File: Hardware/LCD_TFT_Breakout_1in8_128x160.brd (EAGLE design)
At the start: 40.6 x 59.7 mm, 62 parts, among them J1 MICRO-SD_CARD_SOCKETTINY, Q1 220mA/50V/3.5Ω, U2 TXB0108DQSR, U3 3.3V

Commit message: Fix silkscreen and bump out SD card 50 mil
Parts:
- moved U$14 7.62 mm to (15.2, 1.52)
- moved U$29 7.62 mm to (15.2, 1.52)
- moved U$11 2.67 mm to (17.9, 1.52)
- moved U$26 2.67 mm to (17.9, 1.52)
- moved U$12 2.54 mm to (20.3, 1.52)
- moved U$13 2.54 mm to (22.9, 1.52)
- moved U$27 2.54 mm to (20.3, 1.52)
- moved U$28 2.54 mm to (22.9, 1.52)
- moved J1 1.27 mm to (6.35, 19.1)
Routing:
- net 3.3V: track 104.1 -> 107.0 mm
- net MISO: track 23.3 -> 24.6 mm
- net SD_!CS: track 17.6 -> 18.9 mm
- net SCLK: track 30.3 -> 31.5 mm
- net MOSI: track 30.2 -> 31.4 mm
- net GND: vias 31 -> 30

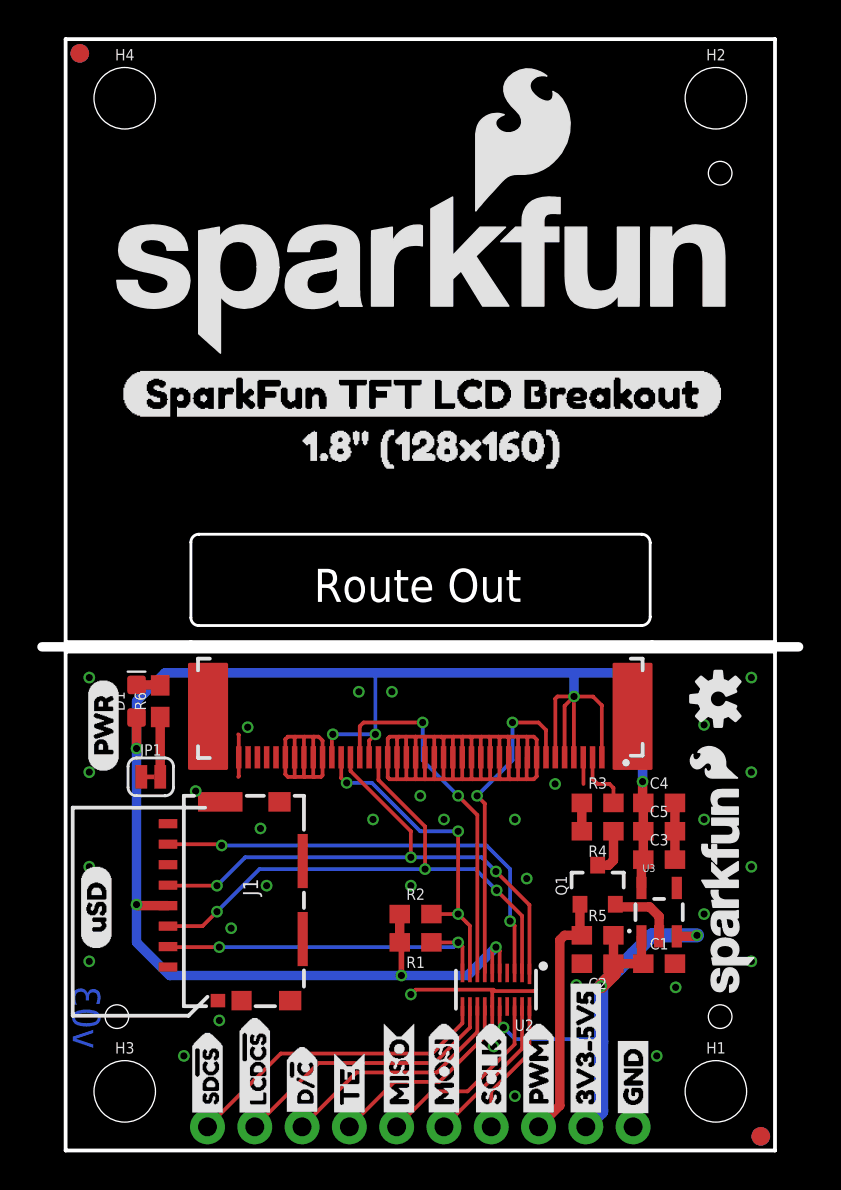
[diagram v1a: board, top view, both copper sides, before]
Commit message: Reduce strain on FPC cable
Acheived by moving the connector toward the PTH row by 40 mil. Route out area moved flush with v-score and also narrowed a little bit
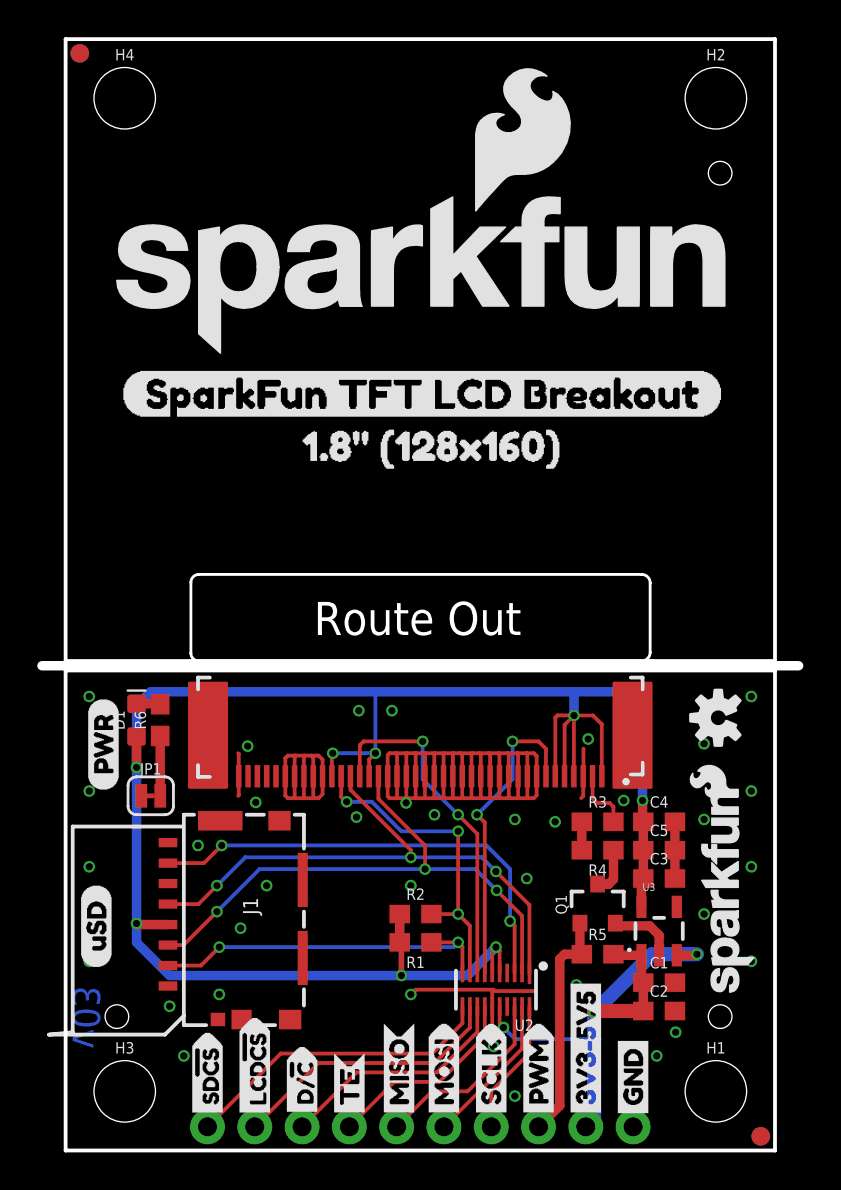
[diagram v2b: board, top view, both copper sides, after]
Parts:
- moved C2 4.17 mm to (31.9, 7.49), turned to 0 degrees
- moved C4 1.02 mm to (31.9, 17.7)
- moved J1 1.02 mm to (6.35, 18.0)
- moved LOGO3 1.02 mm to (35.1, 23.2)
- moved R3 1.02 mm to (28.6, 17.7)
- moved U$18 1.02 mm to (2.03, 19.3)
- moved U$23 1.02 mm to (31.9, 24.5)
- moved C1 1.02 mm to (31.9, 9.02)
- moved C3 1.02 mm to (31.9, 14.6)
- moved Q1 1.02 mm to (28.6, 13.2)
- moved R5 1.02 mm to (28.6, 10.5)
- moved U$4 1.02 mm to (1.65, 9.78)
- moved U3 1.02 mm to (31.9, 11.8)
- moved C5 1.02 mm to (31.9, 16.1)
- moved D1 1.02 mm to (3.81, 23.1)
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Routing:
- net GND: track 90.1 -> 94.0 mm, vias 30 -> 34
- net LED_PWM: track 13.5 -> 12.5 mm
- net D/!C: track 19.8 -> 18.8 mm
- net TE: track 17.8 -> 16.8 mm
- net SCLK: track 31.5 -> 30.9 mm
- net MOSI: track 31.4 -> 30.8 mm
- net 3.3V: track 107.0 -> 106.4 mm
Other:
- outline, holes or cut-outs redrawn

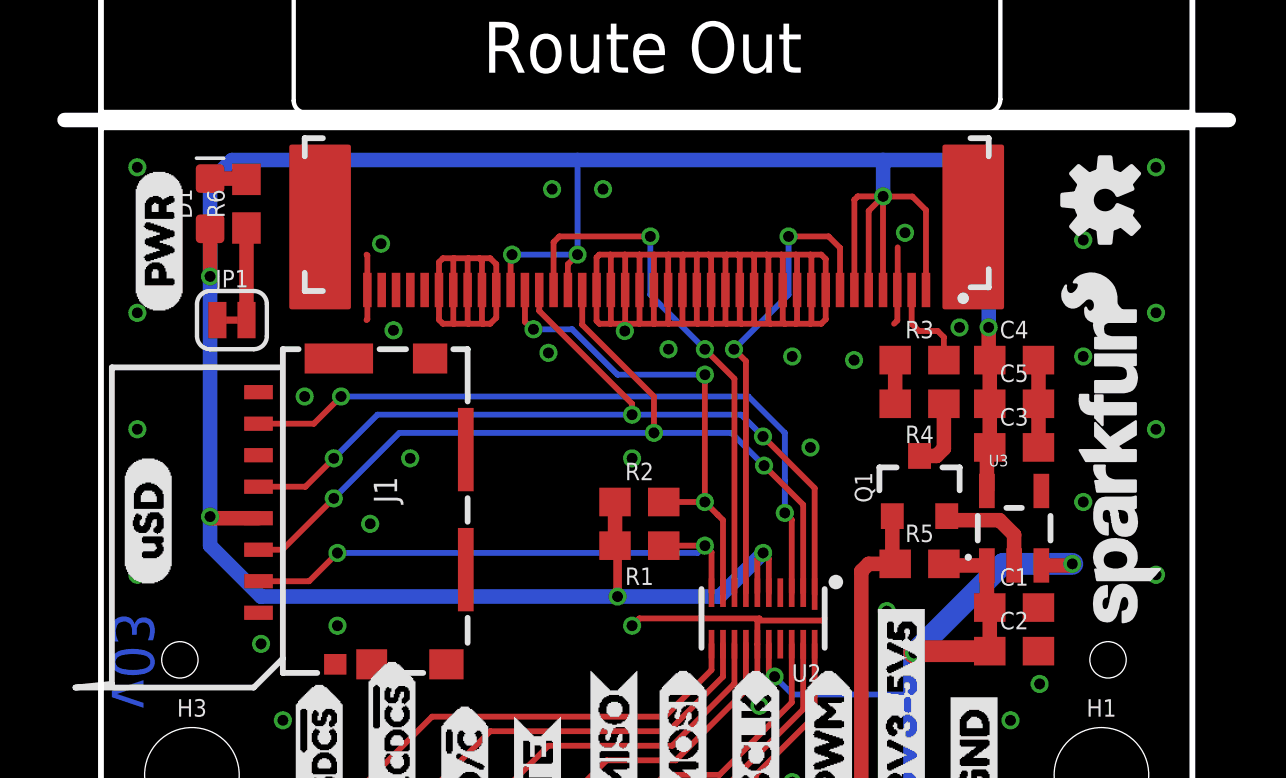
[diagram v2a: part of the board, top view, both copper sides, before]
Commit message: Minor touch-ups (trace routing, silk placement etc)
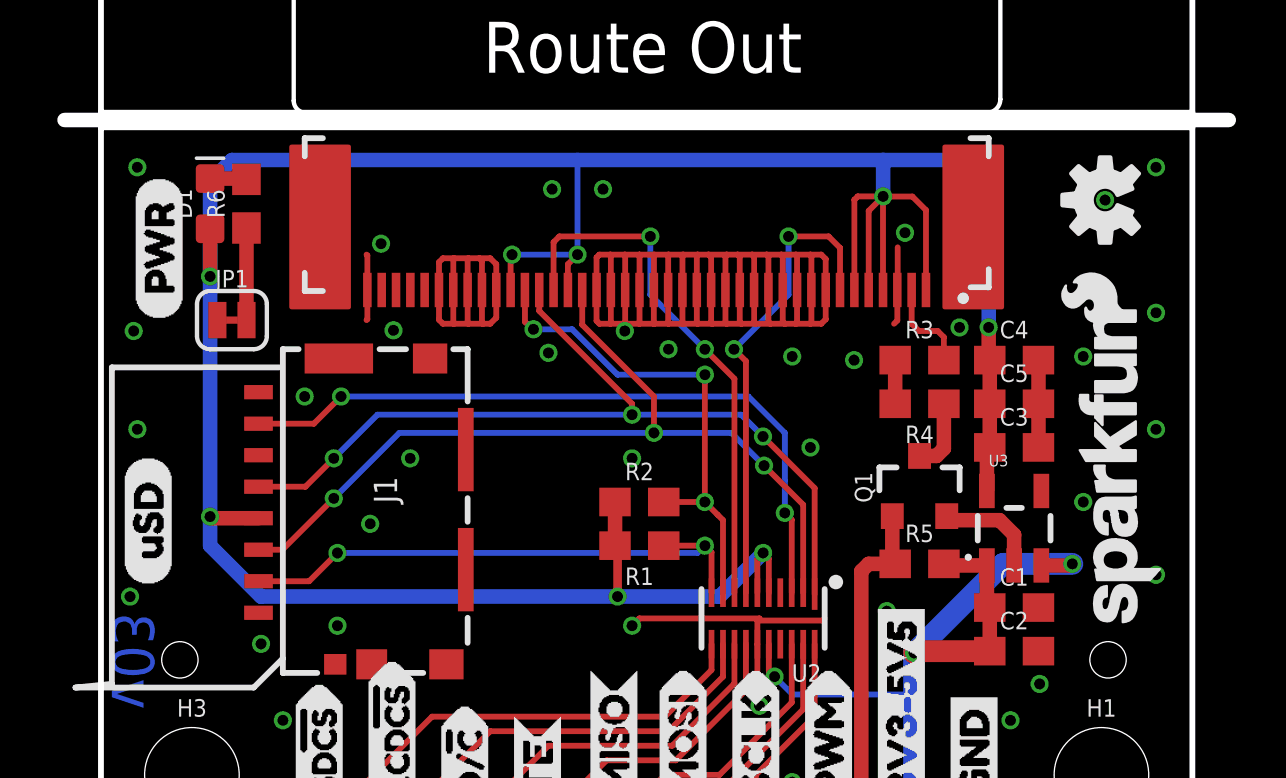
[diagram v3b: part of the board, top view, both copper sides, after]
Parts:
- moved U$18 0.25 mm to (2.03, 19.1)
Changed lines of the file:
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@@
 <attribute name="VALUE" x="4.572" y="17.907" size="0.6096" layer="27" font="vector" ratio="20" align="top-center"/>
 </element>
-<element name="U$18" library="cs" package="PWR4" value="" x="2.032" y="19.304" smashed="yes" rot="R90"/>
+<element name="U$18" library="cs" package="PWR4" value="" x="2.032" y="19.05" smashed="yes" rot="R90"/>
 <element name="U$33" library="SparkFun-Displays" package="KWH018ST14-F01_HOLES" value="EXTERNAL_DISP-KWH018ST14-F01" x="1.905" y="53.34" rot="MR0">
 <attribute name="PROD_ID" value="LCD-14196" x="1.905" y="53.34" size="1.778" layer="28" font="vector" ratio="15" rot="MR0" display="off"/>
@@
 <wire x1="27.8" y1="20.101" x2="27.813" y2="20.088" width="0.2032" layer="1"/>
 <via x="1.27" y="24.384" extent="1-16" drill="0.381"/>
-<via x="1.27" y="19.304" extent="1-16" drill="0.381"/>
+<via x="1.143" y="18.669" extent="1-16" drill="0.381"/>
 <via x="1.27" y="15.24" extent="1-16" drill="0.381"/>
-<via x="1.27" y="10.16" extent="1-16" drill="0.381"/>
+<via x="1.016" y="9.398" extent="1-16" drill="0.381"/>
 <via x="6.35" y="5.08" extent="1-16" drill="0.381"/>
 <via x="8.255" y="8.382" extent="1-16" drill="0.381"/>
-<via x="34.29" y="21.844" extent="1-16" drill="0.381"/>
+<via x="35.052" y="23.241" extent="1-16" drill="0.381"/>
 <via x="36.83" y="24.384" extent="1-16" drill="0.381"/>
 <via x="36.83" y="19.304" extent="1-16" drill="0.381"/>

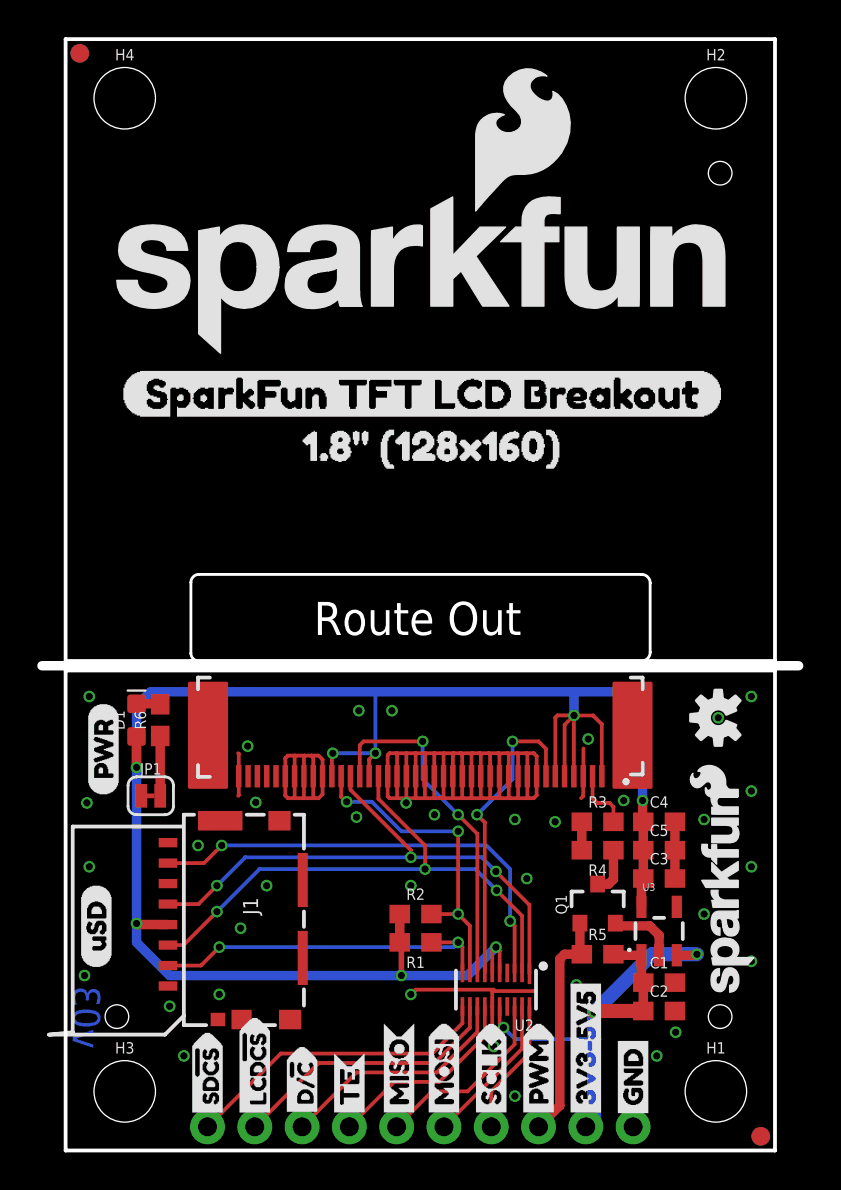
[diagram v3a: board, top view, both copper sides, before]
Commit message: Fixed Reds Design Review Issues
As shown in isse #2
- Offset route-out from v-score
- Added FPC numbers in silk

- Additional little silk rearrangements/tweaking
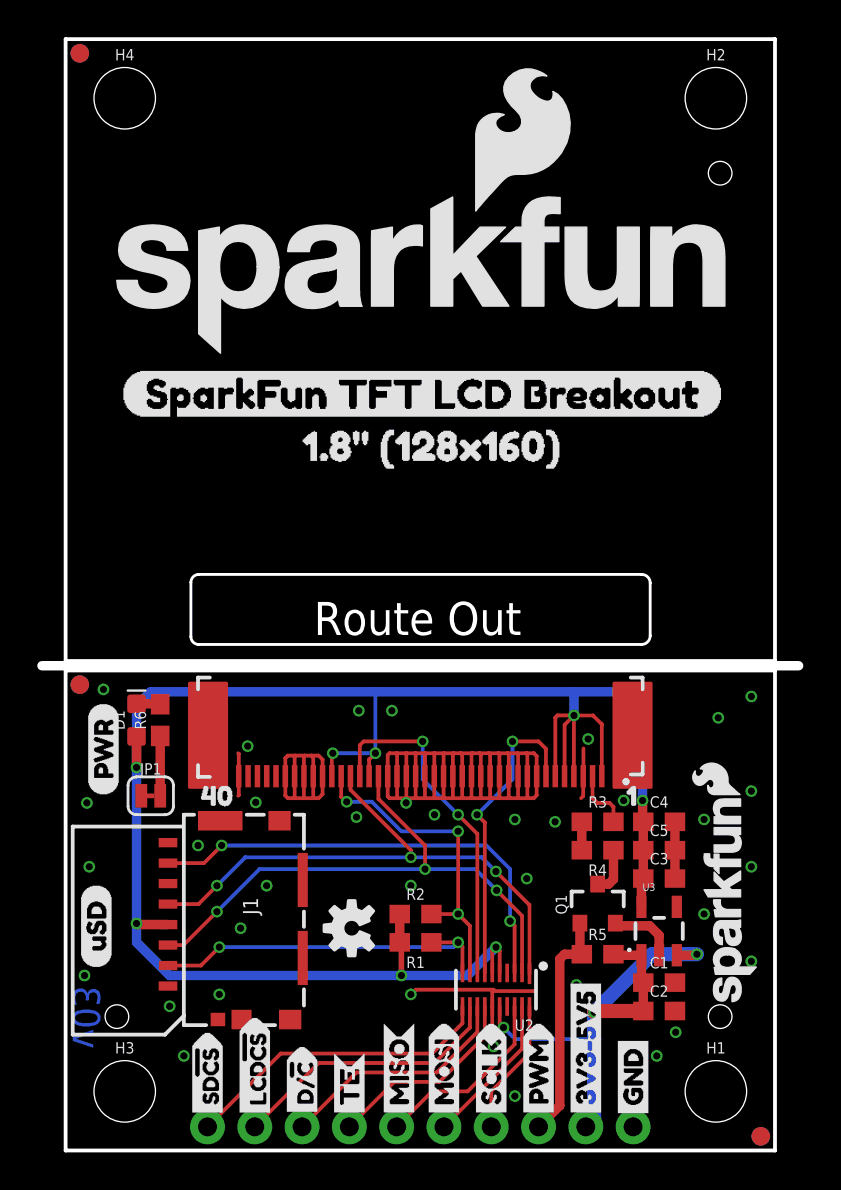
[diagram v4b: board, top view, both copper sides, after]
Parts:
- added FD5, FD6: FIDUCIAL1X2, SparkFun-Aesthetics:FIDUCIAL-1X2
- added U$17: (no value), buzzard_labels:10
- added U$31: (no value), buzzard_labels:401
- moved LOGO3 22.7 mm to (15.4, 11.9)
- moved U$2 0.52 mm to (35.7, 13.5)
- moved U$3 0.18 mm to (34.9, 19.9)
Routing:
- net GND: vias 34 -> 35
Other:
- outline, holes or cut-outs redrawn
